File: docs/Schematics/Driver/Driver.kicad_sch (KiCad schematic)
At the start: 9 parts

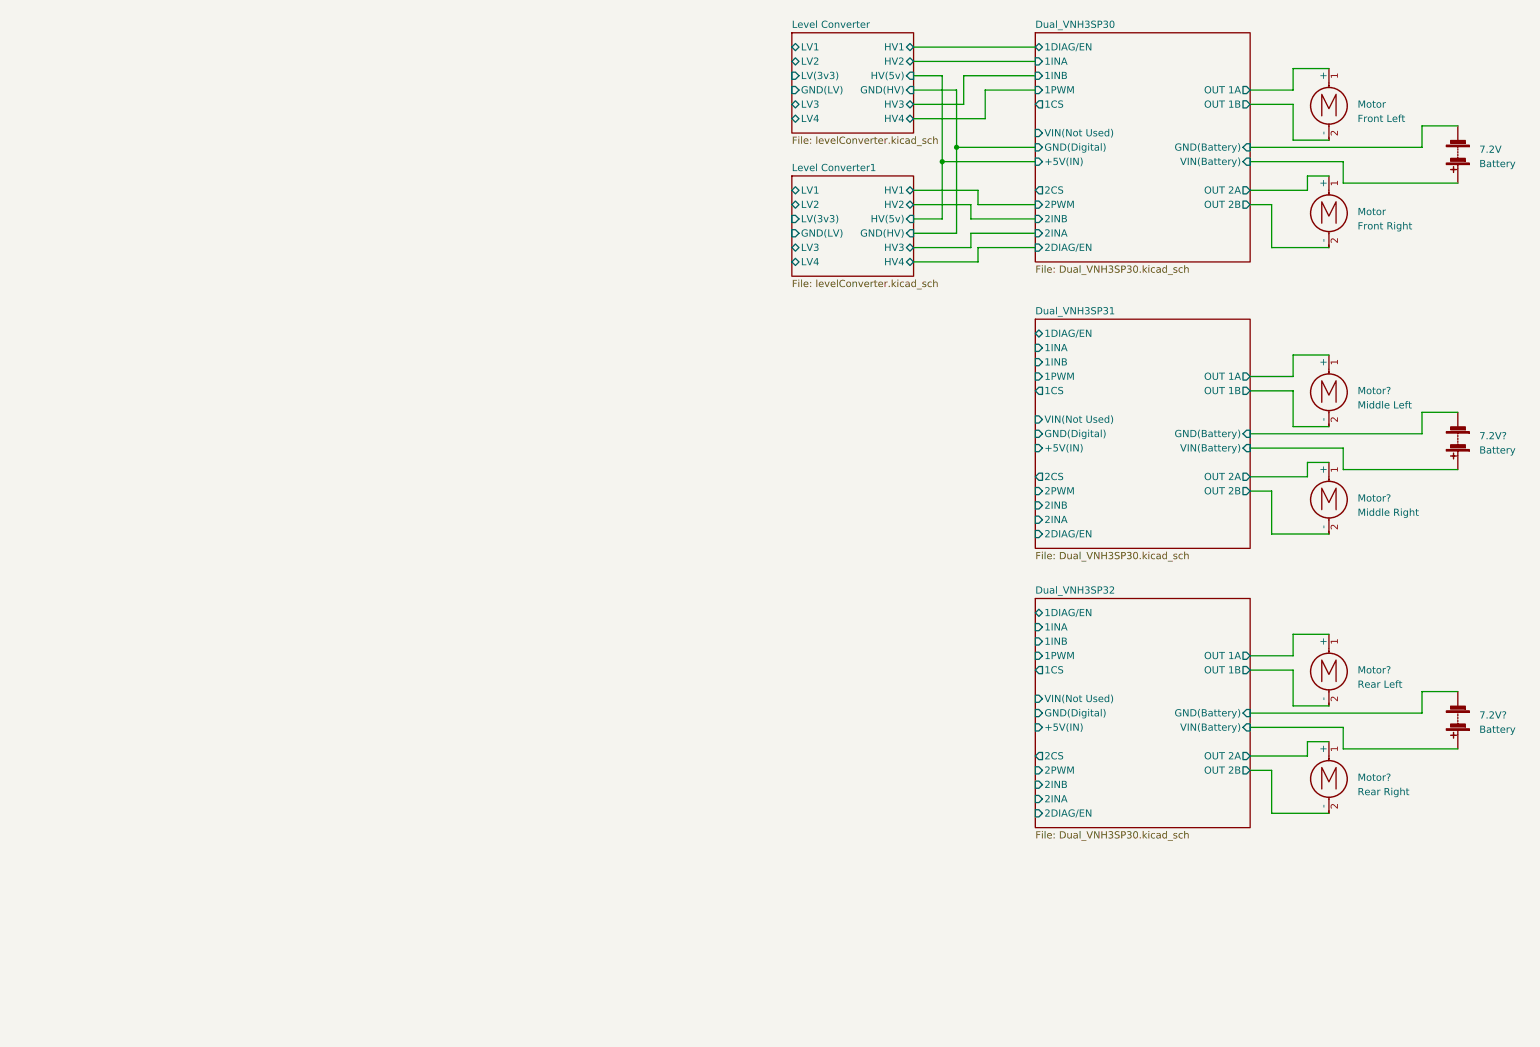
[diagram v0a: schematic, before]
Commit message: Add Wheel encoder
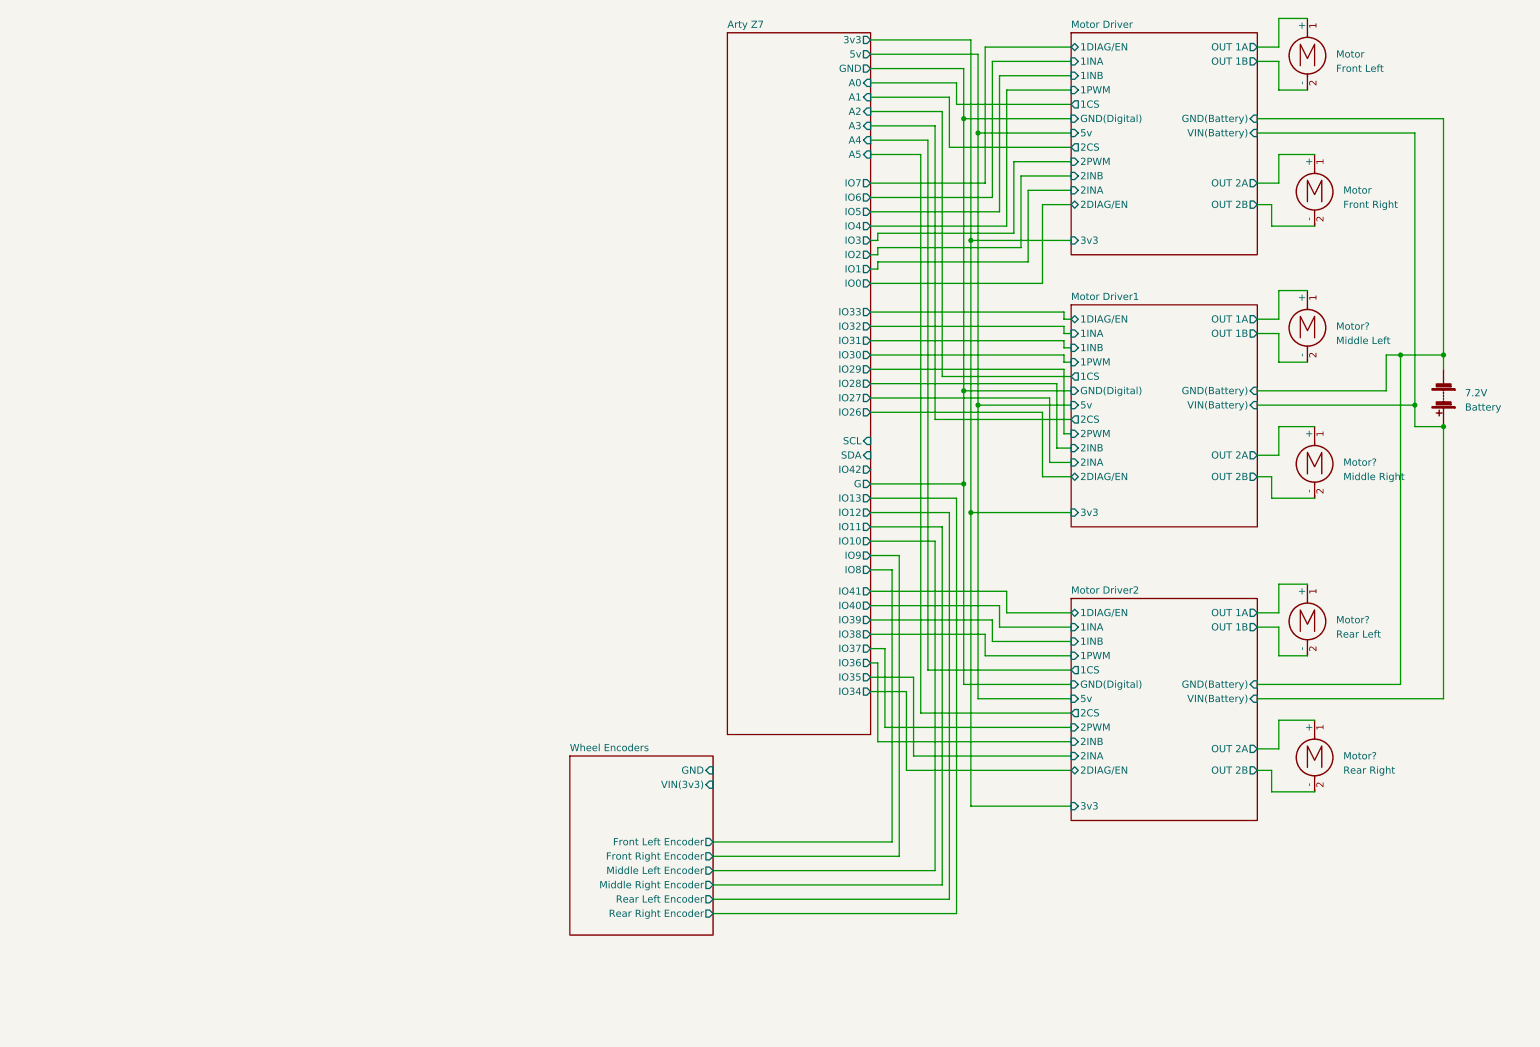
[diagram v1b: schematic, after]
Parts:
- removed 7.2V? (x2): Battery, symbol Device:Battery
- removed Motor?: Rear Right, symbol Motor:Motor_DC
- removed Motor?: Middle Left, symbol Motor:Motor_DC
- removed Motor?: Rear Left, symbol Motor:Motor_DC
- removed Motor?: Middle Right, symbol Motor:Motor_DC
- added Motor?: Rear Left, symbol Motor:Motor_DC
- added Motor?: Middle Right, symbol Motor:Motor_DC
- added Motor?: Middle Left, symbol Motor:Motor_DC
- added Motor?: Rear Right, symbol Motor:Motor_DC
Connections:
- net Dual_VNH3SP30/GND(Battery) renamed Motor Driver/GND(Battery)
- net Dual_VNH3SP30/OUT 1A renamed Motor Driver/OUT 1A
- net Dual_VNH3SP30/OUT 1B renamed Motor Driver/OUT 1B
- net Dual_VNH3SP30/OUT 2A renamed Motor Driver/OUT 2A
- net Dual_VNH3SP30/OUT 2B renamed Motor Driver/OUT 2B
- net Dual_VNH3SP30/VIN(Battery) renamed Motor Driver/VIN(Battery)
- new net Motor Driver1/OUT 1A: Motor?.1 (+)
- new net Motor Driver1/OUT 1B: Motor?.2 (-)
- new net Motor Driver1/OUT 2A: Motor?.1 (+)
- new net Motor Driver1/OUT 2B: Motor?.2 (-)
- new net Motor Driver2/OUT 1A: Motor?.1 (+)
- new net Motor Driver2/OUT 1B: Motor?.2 (-)
- new net Motor Driver2/OUT 2A: Motor?.1 (+)
- new net Motor Driver2/OUT 2B: Motor?.2 (-)
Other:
- removed sheet Dual_VNH3SP30
- removed sheet Dual_VNH3SP31
- removed sheet Dual_VNH3SP32
- removed sheet Level Converter
- removed sheet Level Converter1
- added sheet Arty Z7 (ArtyZ7.kicad_sch)
- added sheet Motor Driver (motorDriver.kicad_sch)
- added sheet Motor Driver1 (motorDriver.kicad_sch)
- added sheet Motor Driver2 (motorDriver.kicad_sch)
- added sheet Wheel Encoders (wheelEncoders.kicad_sch)
- moved on the sheet: 7.2V, Motor

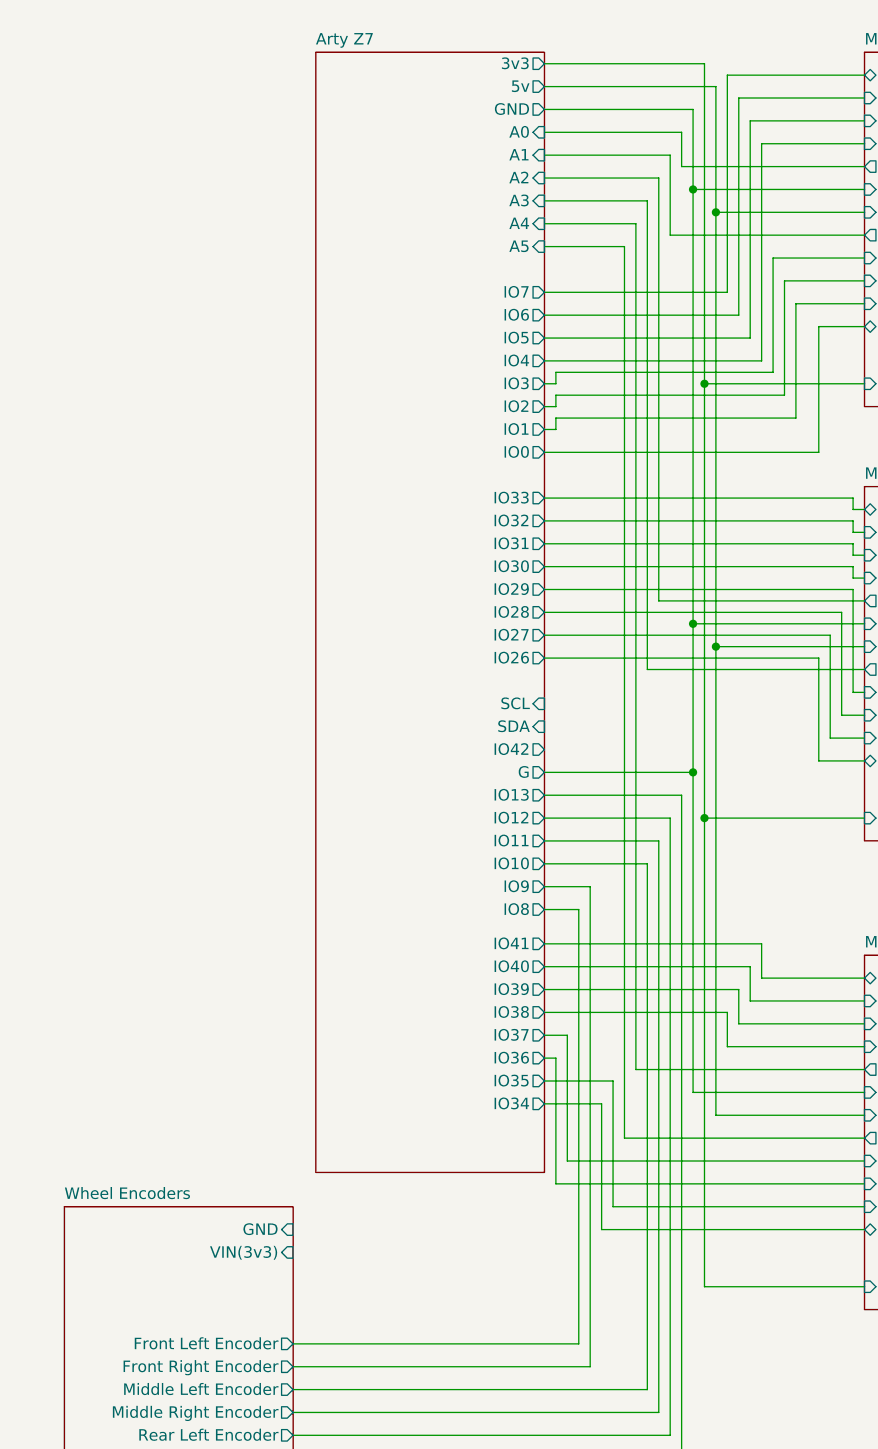
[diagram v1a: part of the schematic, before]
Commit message: Added esp32HB and oled
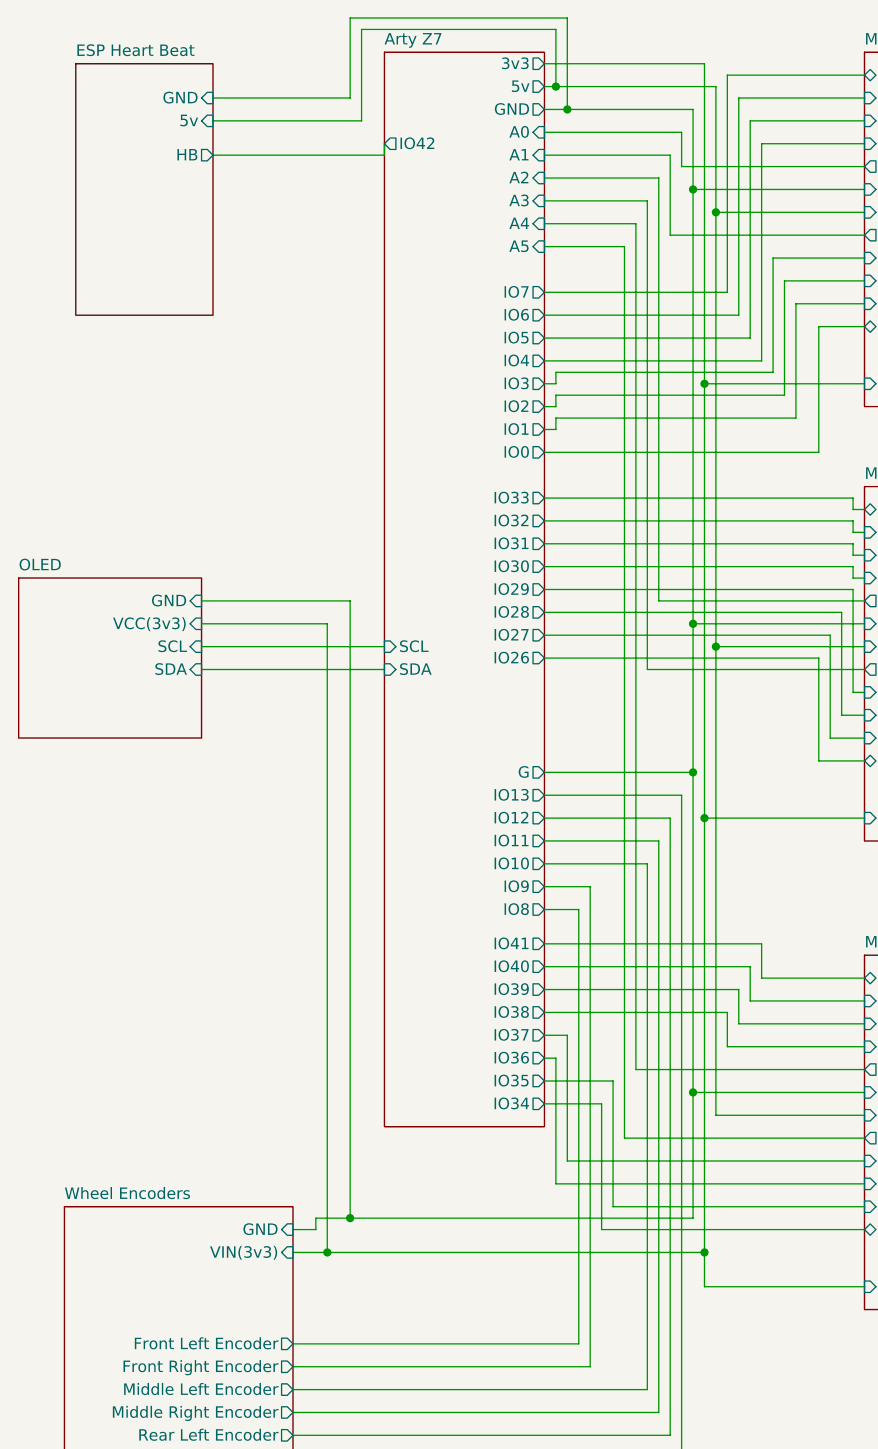
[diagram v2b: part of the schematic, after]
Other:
- added sheet ESP Heart Beat (espHeartBeat.kicad_sch)
- added sheet OLED (oled.kicad_sch)

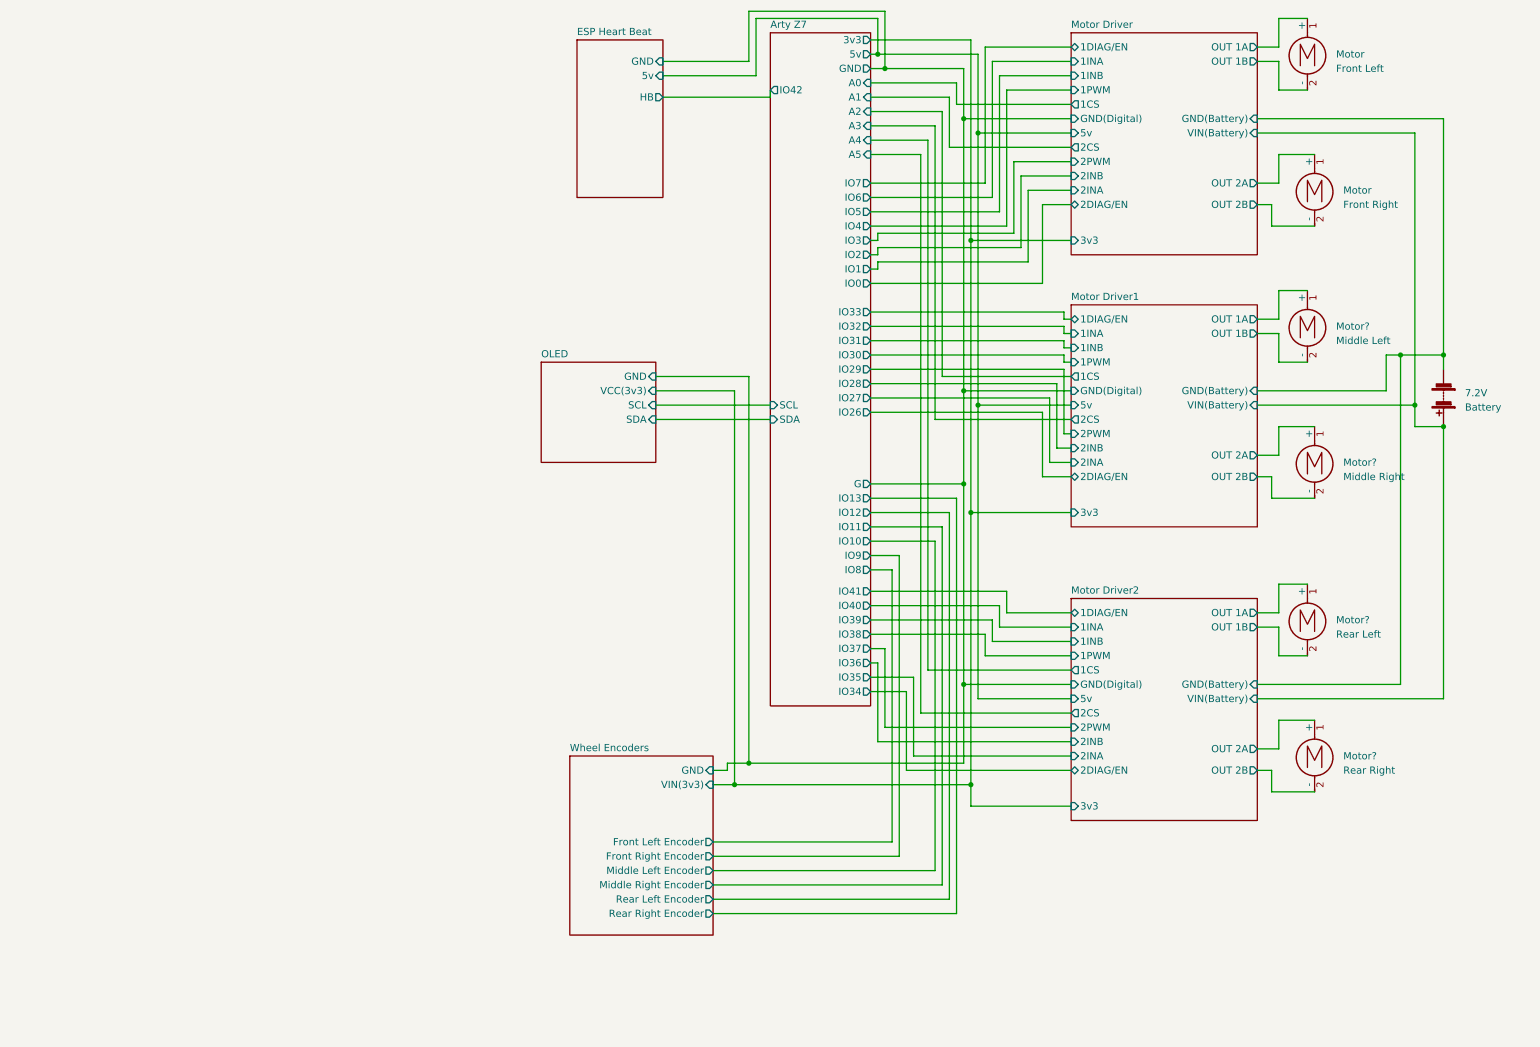
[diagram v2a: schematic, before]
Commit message: First scematic design for the card
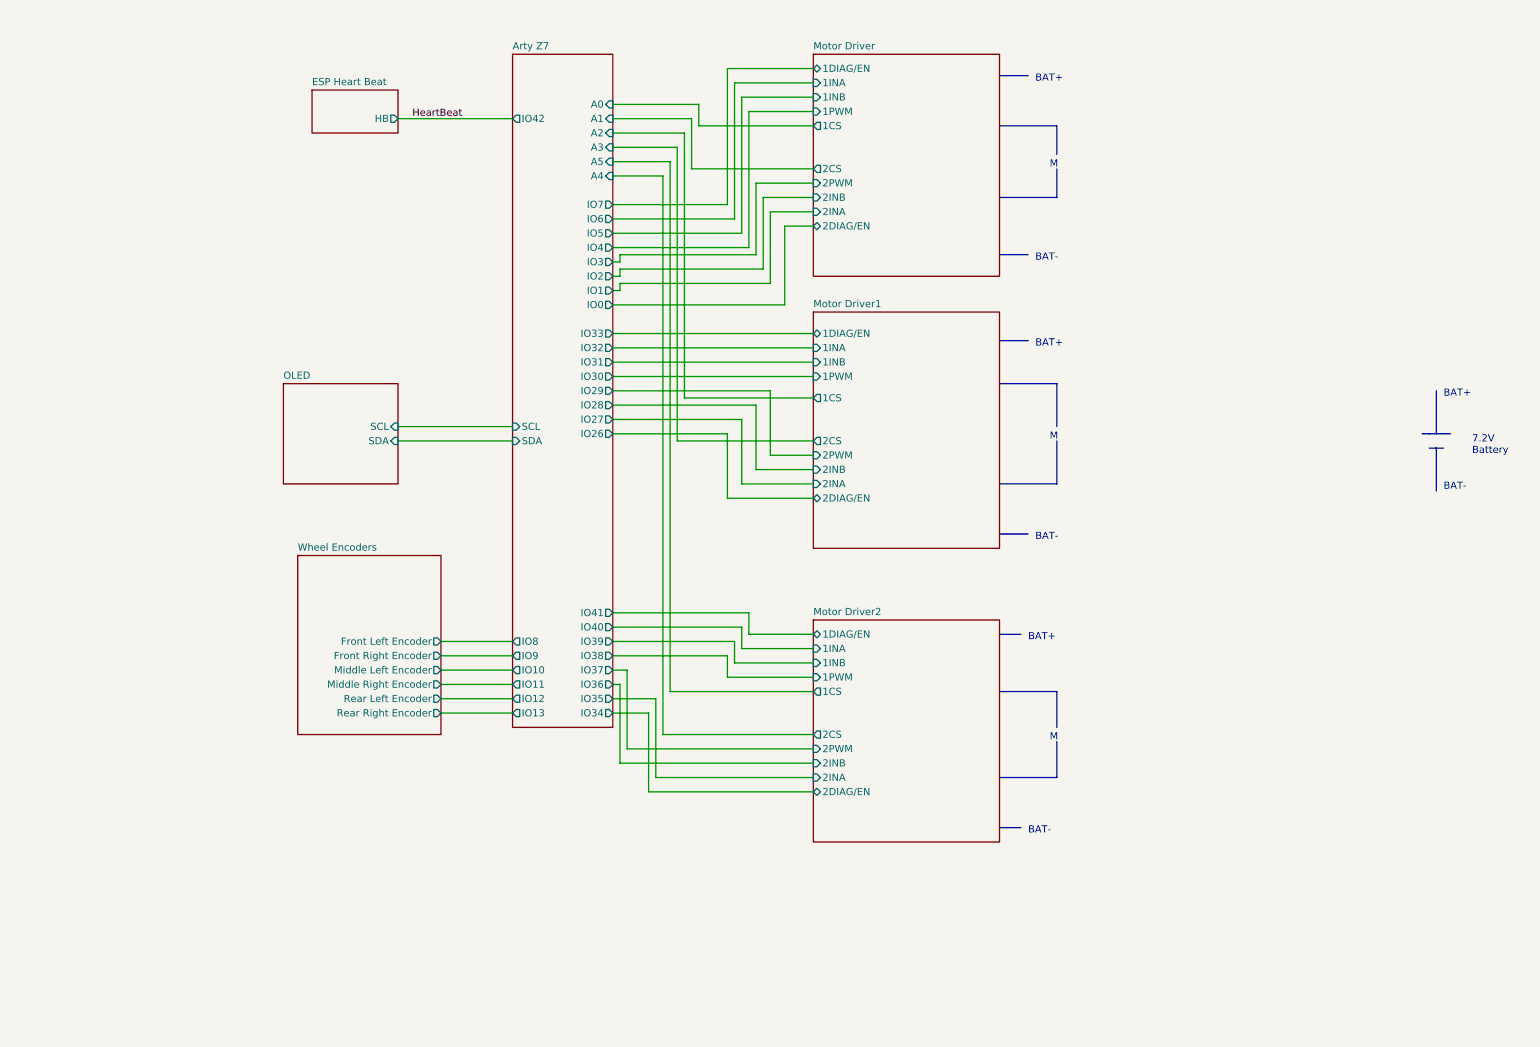
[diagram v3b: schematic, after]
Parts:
- removed 7.2V: Battery, symbol Device:Battery
- removed Motor: Front Left, symbol Motor:Motor_DC
- removed Motor: Front Right, symbol Motor:Motor_DC
- removed Motor?: Rear Left, symbol Motor:Motor_DC
- removed Motor?: Middle Right, symbol Motor:Motor_DC
- removed Motor?: Middle Left, symbol Motor:Motor_DC
- removed Motor?: Rear Right, symbol Motor:Motor_DC
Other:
- sheet Arty Z7 ports: added none; removed 3v3, 5v, G, GND
- sheet ESP Heart Beat ports: added none; removed 5v, GND
- sheet Motor Driver ports: added none; removed 3v3, 5v, GND(Battery), GND(Digital), OUT 1A, OUT 1B, OUT 2A, OUT 2B, VIN(Battery)
- sheet Motor Driver1 ports: added none; removed 3v3, 5v, GND(Battery), GND(Digital), OUT 1A, OUT 1B, OUT 2A, OUT 2B, VIN(Battery)
- sheet Motor Driver2 ports: added none; removed 3v3, 5v, GND(Battery), GND(Digital), OUT 1A, OUT 1B, OUT 2A, OUT 2B, VIN(Battery)
- sheet OLED ports: added none; removed GND, VCC(3v3)
- sheet Wheel Encoders ports: added none; removed GND, VIN(3v3)
- note added: "7.2V Battery"
- note added: "BAT+"
- note added: "BAT-"
- note added: "M"
- company: (none) -> HiQ
- title: (none) -> Arty Z7 IO expander card
